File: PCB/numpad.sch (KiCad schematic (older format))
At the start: 65 parts, among them J1 AVR-ISP-6, J2 Conn_01x04_Female, SW1 SW_Push, U1 ProMicro

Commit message: Added mounting holes
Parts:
- added H1, H2, H3, H4: Hole, MountingHole:MountingHole_3.2mm_M3_Pad, symbol Mechanical:MountingHole_Pad
- MX11, MX15, MX17: footprint CherryMX_KailhSocket_StabWireBottom_LTST-A683CEGBW:CherryMX_2.00u_KailhSocket_StabWireBottom_LTST-A683CEGBW -> CherryMX_PCB_KailhSocket_StabWireBottom_LTST-A683CEGBW:CherryMX_2.00u_PCB_KailhSocket_StabWireBottom_LTST-A683CEGBW
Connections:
- net GND: now also H1.1, H2.1, H3.1, H4.1
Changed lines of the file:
@@
 F 0 "MX11" H 9800 4085 50  0000 C CNN
 F 1 "+" H 9800 3994 50  0000 C CNN
-F 2 "CherryMX_KailhSocket_StabWireBottom_LTST-A683CEGBW:CherryMX_2.00u_KailhSocket_StabWireBottom_LTST-A683CEGBW" H 9800 3600 50  0001 C CNN
+F 2 "CherryMX_PCB_KailhSocket_StabWireBottom_LTST-A683CEGBW:CherryMX_2.00u_PCB_KailhSocket_StabWireBottom_LTST-A683CEGBW" H 9800 3600 50  0001 C CNN
 F 3 "" H 9800 3600 50  0001 C CNN
 F 4 "0" H 9800 3700 50  0001 C CNN "JLCPCB BOM"
@@
 F 0 "MX15" H 4700 6035 50  0000 C CNN
 F 1 "0" H 4700 5944 50  0000 C CNN
-F 2 "CherryMX_KailhSocket_StabWireBottom_LTST-A683CEGBW:CherryMX_2.00u_KailhSocket_StabWireBottom_LTST-A683CEGBW" H 4700 5550 50  0001 C CNN
+F 2 "CherryMX_PCB_KailhSocket_StabWireBottom_LTST-A683CEGBW:CherryMX_2.00u_PCB_KailhSocket_StabWireBottom_LTST-A683CEGBW" H 4700 5550 50  0001 C CNN
 F 3 "" H 4700 5550 50  0001 C CNN
 F 4 "0" H 4700 5650 50  0001 C CNN "JLCPCB BOM"
@@
 F 0 "MX17" H 8100 6035 50  0000 C CNN
 F 1 "Enter" H 8100 5944 50  0000 C CNN
-F 2 "CherryMX_KailhSocket_StabWireBottom_LTST-A683CEGBW:CherryMX_2.00u_KailhSocket_StabWireBottom_LTST-A683CEGBW" H 8100 5550 50  0001 C CNN
+F 2 "CherryMX_PCB_KailhSocket_StabWireBottom_LTST-A683CEGBW:CherryMX_2.00u_PCB_KailhSocket_StabWireBottom_LTST-A683CEGBW" H 8100 5550 50  0001 C CNN
 F 3 "" H 8100 5550 50  0001 C CNN
 F 4 "0" H 8100 5650 50  0001 C CNN "JLCPCB BOM"
@@
 Wire Wire Line
 	10100 2700 10550 2700
+$Comp
+L Mechanical:MountingHole_Pad H1
+U 1 1 6510CF3E
+P 4400 6900
+F 0 "H1" H 4500 6949 50  0000 L CNN
+F 1 "Hole" H 4500 6858 50  0000 L CNN
+F 2 "MountingHole:MountingHole_3.2mm_M3_Pad" H 4400 6900 50  0001 C CNN
+F 3 "~" H 4400 6900 50  0001 C CNN
+	1    4400 6900
+	1    0    0    -1
+$EndComp
+$Comp
+L power:GND #PWR0103
+U 1 1 6510E1D6
+P 5550 7100
+F 0 "#PWR0103" H 5550 6850 50  0001 C CNN
+F 1 "GND" H 5555 6927 50  0000 C CNN
+F 2 "" H 5550 7100 50  0001 C CNN
+F 3 "" H 5550 7100 50  0001 C CNN
+	1    5550 7100
+	1    0    0    -1
+$EndComp
+$Comp
+L Mechanical:MountingHole_Pad H2
+U 1 1 6510E748
+P 4750 6900
+F 0 "H2" H 4850 6949 50  0000 L CNN
+F 1 "Hole" H 4850 6858 50  0000 L CNN
+F 2 "MountingHole:MountingHole_3.2mm_M3_Pad" H 4750 6900 50  0001 C CNN
+F 3 "~" H 4750 6900 50  0001 C CNN
+	1    4750 6900
+	1    0    0    -1
+$EndComp
+$Comp
+L Mechanical:MountingHole_Pad H3
+U 1 1 6510E899
+P 5100 6900
+F 0 "H3" H 5200 6949 50  0000 L CNN
+F 1 "Hole" H 5200 6858 50  0000 L CNN
+F 2 "MountingHole:MountingHole_3.2mm_M3_Pad" H 5100 6900 50  0001 C CNN
+F 3 "~" H 5100 6900 50  0001 C CNN
+	1    5100 6900
+	1    0    0    -1
+$EndComp
+$Comp
+L Mechanical:MountingHole_Pad H4
+U 1 1 6510EA43
+P 5450 6900
+F 0 "H4" H 5550 6949 50  0000 L CNN
+F 1 "Hole" H 5550 6858 50  0000 L CNN
+F 2 "MountingHole:MountingHole_3.2mm_M3_Pad" H 5450 6900 50  0001 C CNN
+F 3 "~" H 5450 6900 50  0001 C CNN
+	1    5450 6900
+	1    0    0    -1
+$EndComp
+Wire Wire Line
+	5450 7000 5100 7000
+Connection ~ 4750 7000
+Wire Wire Line
+	4750 7000 4400 7000
+Connection ~ 5100 7000
+Wire Wire Line
+	5100 7000 4750 7000
+Wire Wire Line
+	5450 7000 5550 7000
+Wire Wire Line
+	5550 7000 5550 7100
+Connection ~ 5450 7000
 $EndSCHEMATC

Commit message: Exported gerbers
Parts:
- H1, H2, H3, H4: JLCPCB BOM (none) -> 0
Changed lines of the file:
@@
 F 2 "MountingHole:MountingHole_3.2mm_M3_Pad" H 4400 6900 50  0001 C CNN
 F 3 "~" H 4400 6900 50  0001 C CNN
+F 4 "0" H 4400 6900 50  0001 C CNN "JLCPCB BOM"
 	1    4400 6900
 	1    0    0    -1
@@
 F 2 "MountingHole:MountingHole_3.2mm_M3_Pad" H 4750 6900 50  0001 C CNN
 F 3 "~" H 4750 6900 50  0001 C CNN
+F 4 "0" H 4750 6900 50  0001 C CNN "JLCPCB BOM"
 	1    4750 6900
 	1    0    0    -1
@@
 F 2 "MountingHole:MountingHole_3.2mm_M3_Pad" H 5100 6900 50  0001 C CNN
 F 3 "~" H 5100 6900 50  0001 C CNN
+F 4 "0" H 5100 6900 50  0001 C CNN "JLCPCB BOM"
 	1    5100 6900
 	1    0    0    -1
@@
 F 2 "MountingHole:MountingHole_3.2mm_M3_Pad" H 5450 6900 50  0001 C CNN
 F 3 "~" H 5450 6900 50  0001 C CNN
+F 4 "0" H 5450 6900 50  0001 C CNN "JLCPCB BOM"
 	1    5450 6900
 	1    0    0    -1

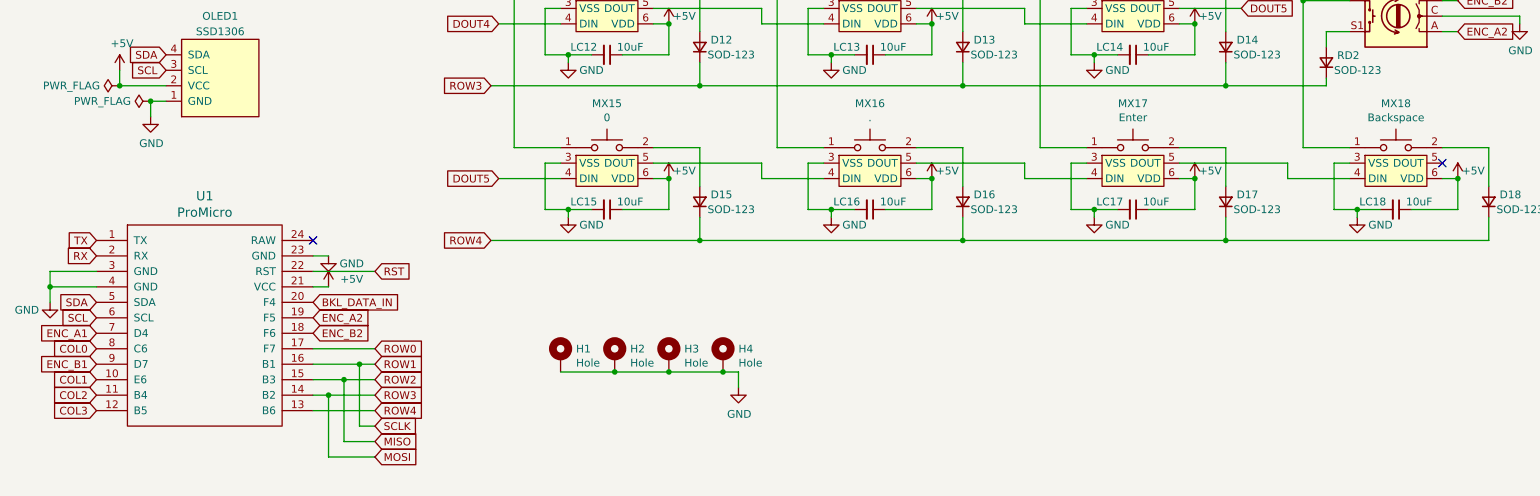
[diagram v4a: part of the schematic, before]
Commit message: Added logos, cleaned up routing
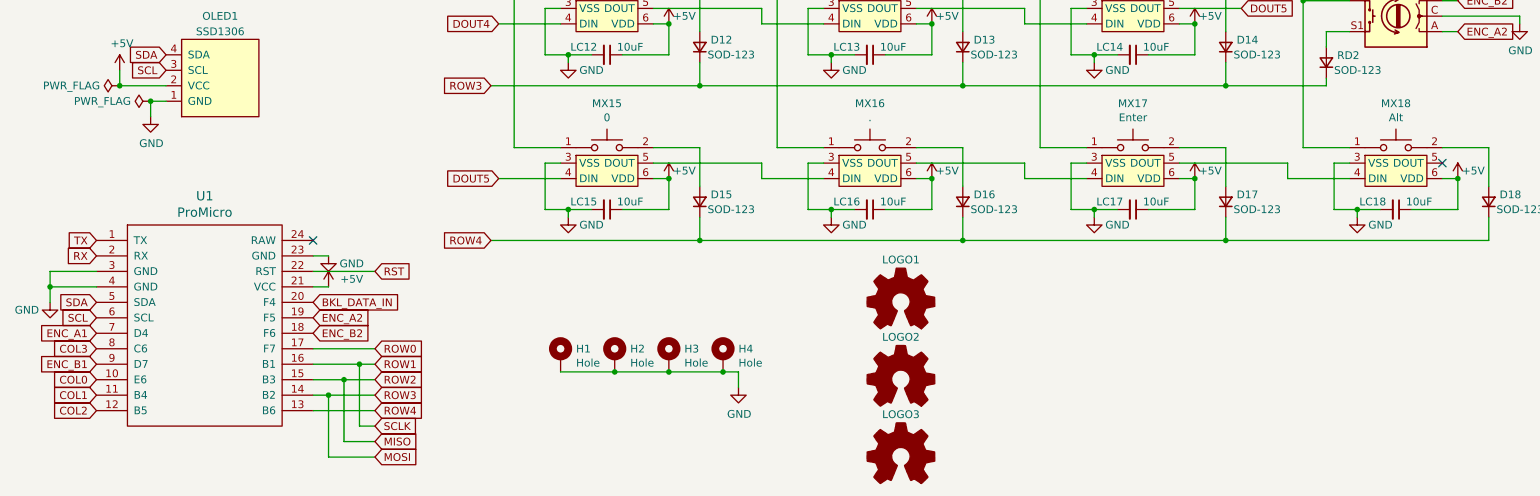
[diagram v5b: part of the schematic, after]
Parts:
- added LOGO1: Logo_Open_Hardware_Small, custom_footprints:logo, symbol Graphic:Logo_Open_Hardware_Small
- added LOGO2: Logo_Open_Hardware_Small, custom_footprints:qmk_logo, symbol Graphic:Logo_Open_Hardware_Small
- added LOGO3: Logo_Open_Hardware_Small, custom_footprints:vial_logo, symbol Graphic:Logo_Open_Hardware_Small
- D1, D10, D11, D12, D13, D14, D15, D16, D17, D18, D2, D3, D4, D5, D6, D7, D8, D9, RD1, RD2: footprint Diode_SMD:D_SOD-123 -> Diode_SMD:D_SOD-323_HandSoldering; LCSC Part C81598 -> C2128
- MX1, MX10, MX11, MX12, MX13, MX14, MX15, MX16, MX17, MX2, MX3, MX4, MX5, MX6, MX7, MX8, MX9: JLCPCB BOM 0 -> (none); LCSC Part (none) -> C524051
- MX18: value Backspace -> Alt; footprint CherryMX_PCB_KailhSocket_LTST-A683CEGBW:CherryMX_1.00u_PCB_KailhSocket_LTST-A683CEGBW -> CherryMX_PCB_KailhSocket_LTST-A683CEGBW:CherryMX_1.50u_PCB_KailhSocket_LTST-A683CEGBW; JLCPCB BOM 0 -> (none); LCSC Part (none) -> C524051
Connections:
- net COL0: now also U1.10 (E6); no longer U1.8 (C6)
- net COL1: now also U1.11 (B4); no longer U1.10 (E6)
- net COL2: now also U1.12 (B5); no longer U1.11 (B4)
- net COL3: now also U1.8 (C6); no longer U1.12 (B5)
